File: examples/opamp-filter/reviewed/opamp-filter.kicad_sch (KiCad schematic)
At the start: 27 parts, among them J1 IN, J2 5V, J3 OUT, U1 MCP6001R, U2 MCP6001R

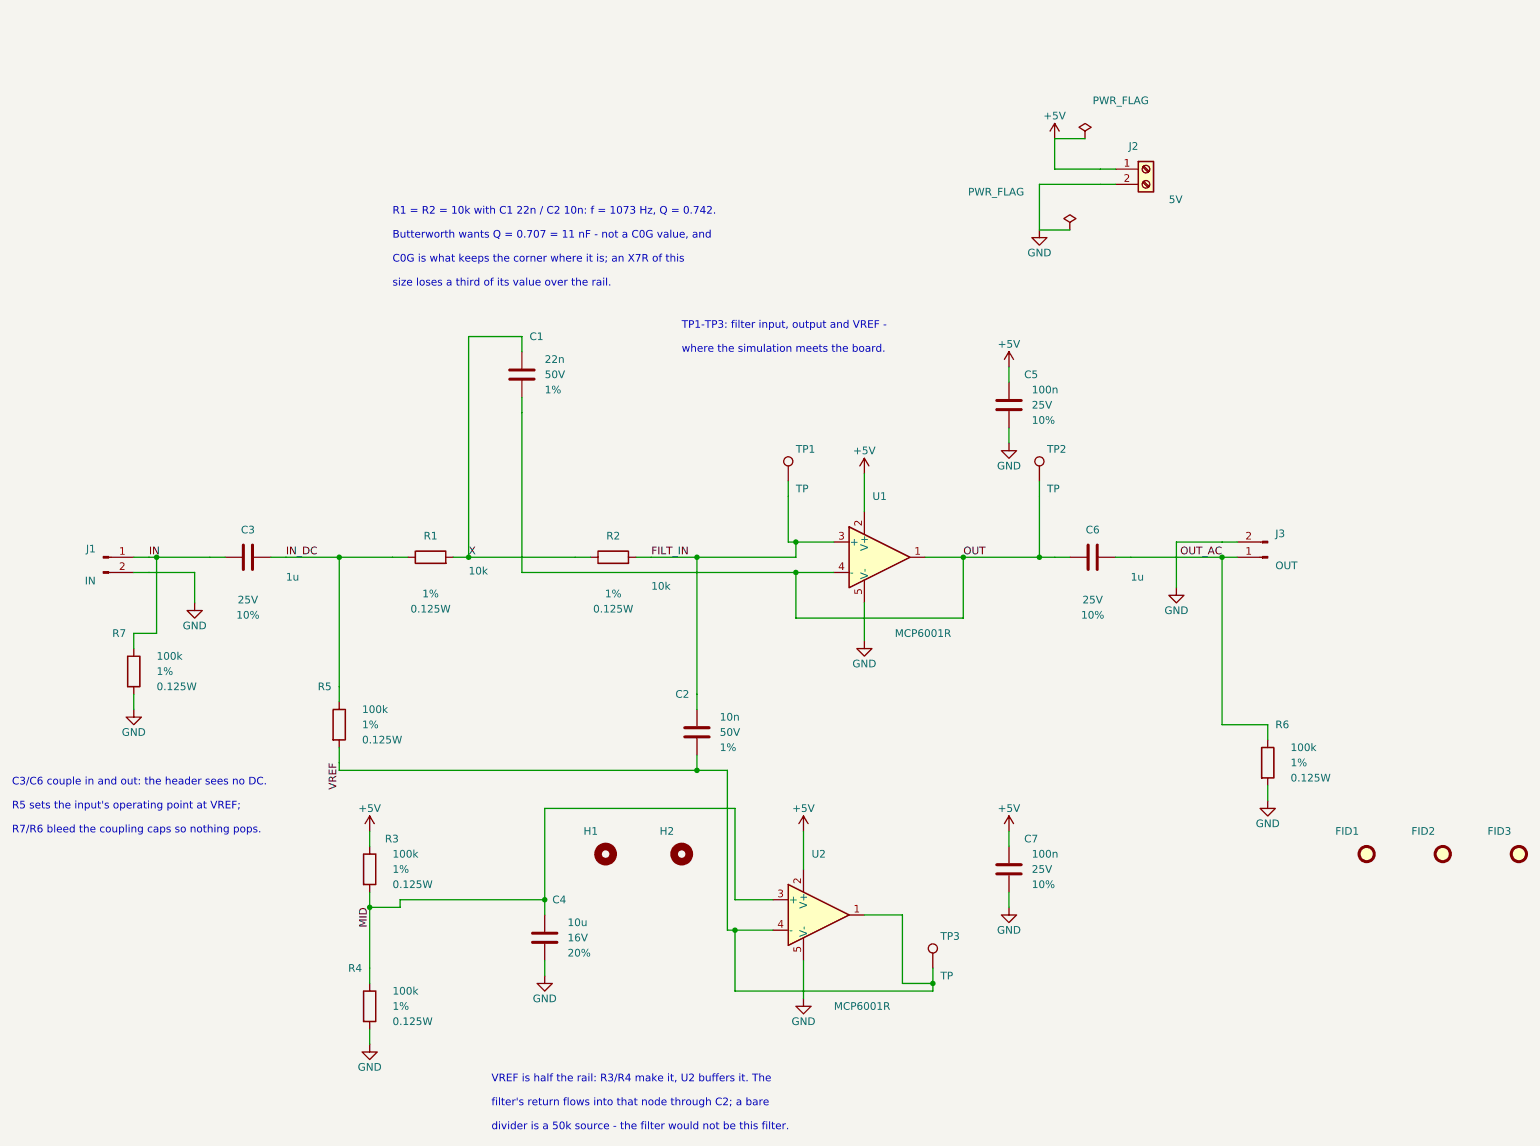
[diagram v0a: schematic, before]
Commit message: chore(examples): regenerate the four two-layer boards and their pictures
buck-5v, motor-driver, pico-carrier and opamp-filter, regenerated from the
merged generator and gated clean on KiCad 9.0.9. The inner-layer pictures go
with the inner layers.

fpga-audio is still routing; it follows.

Co-Authored-By: Claude Opus 5 <noreply@anthropic.com>
Claude-Session: https://claude.ai/code/session_01XQE7UkE9WTSMW3oZ3kLeCt
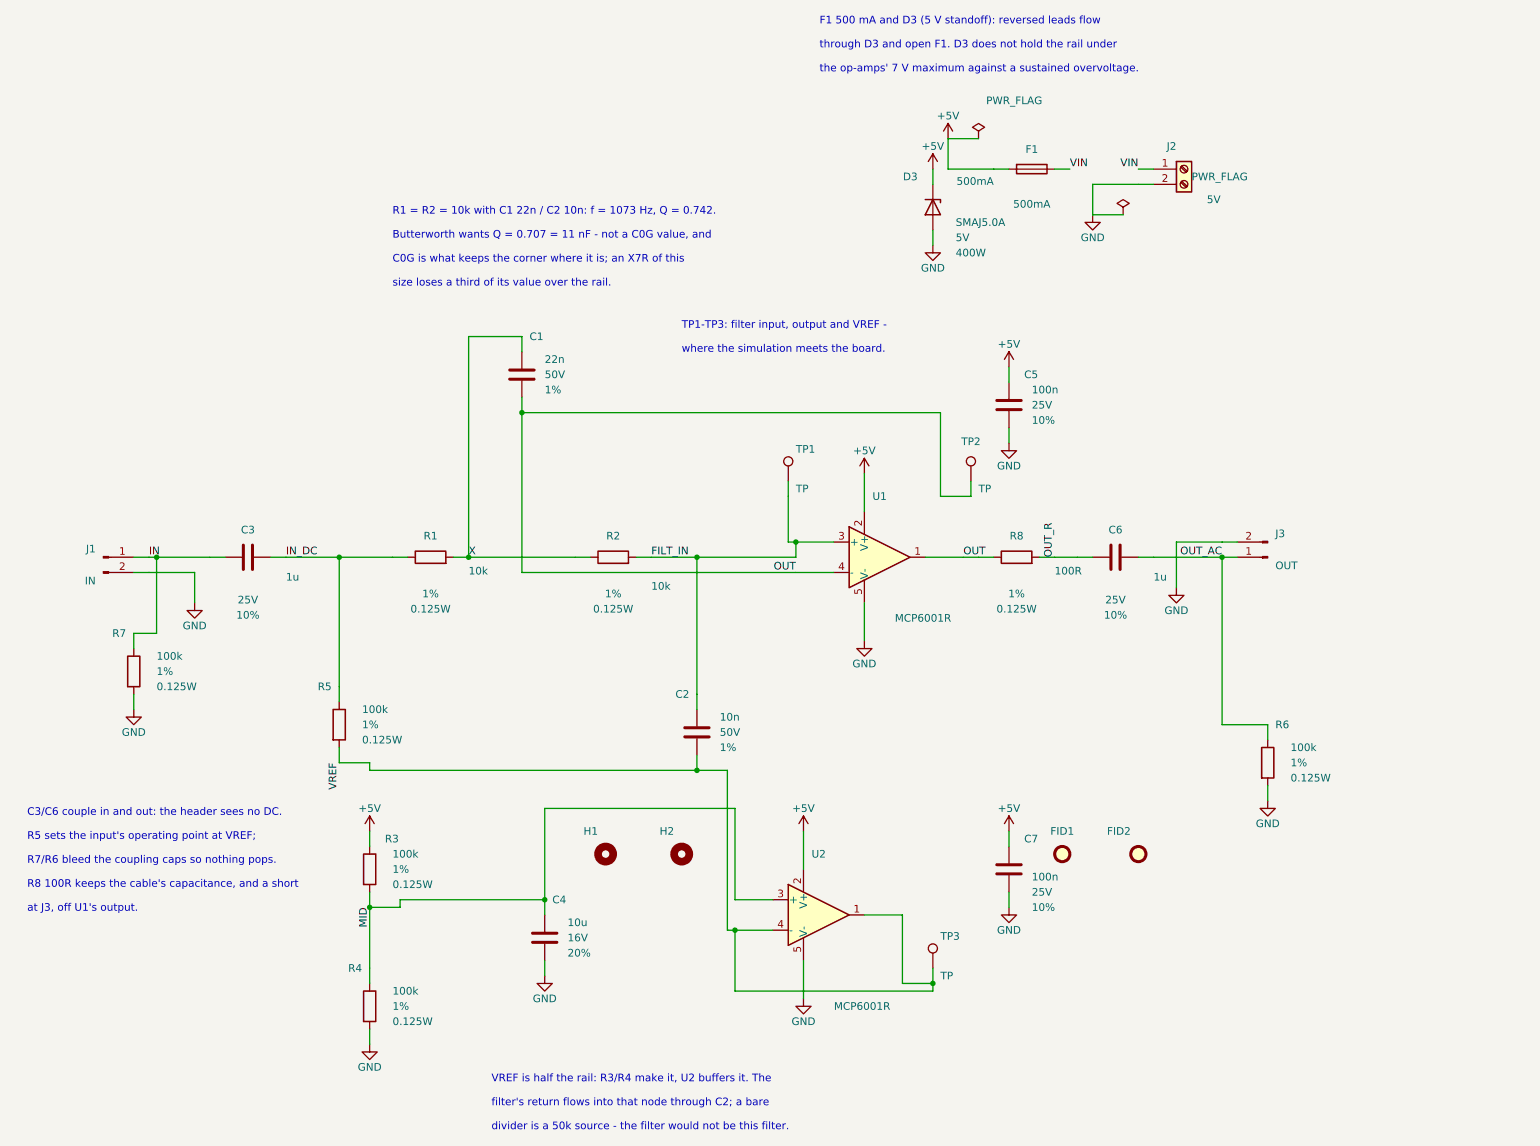
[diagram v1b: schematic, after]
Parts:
- removed FID3: Fiducial, Fiducial:Fiducial_1mm_Mask2mm, symbol Mechanical:Fiducial
- added D3: SMAJ5.0A, Diode_SMD:D_SMA, symbol Device:D_Zener
- added F1: 500mA, Fuse:Fuse_1206_3216Metric, symbol Device:Fuse
- added R8: 100R, Resistor_SMD:R_0805_2012Metric, symbol Device:R
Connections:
- net +5V: now also D3.1 (K), F1.2; no longer J2.1 (Pin_1)
- net GND: now also D3.2 (A)
- net OUT: now also R8.1; no longer C6.1
- new net OUT_R: C6.1, R8.2
- new net VIN: F1.1, J2.1 (Pin_1)
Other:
- note added: "F1 500 mA and D3 (5 V standoff): reversed leads flow"
- note added: "R8 100R keeps the cable's capacitance, and a short"
- note added: "at J3, off U1's output."
- note added: "the op-amps' 7 V maximum against a sustained overvoltage."
- note added: "through D3 and open F1. D3 does not hold the rail under"
- moved on the sheet: C6, FID1, FID2, J2, TP2
